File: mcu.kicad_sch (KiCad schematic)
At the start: 36 parts, among them Q1 BC817, Q2 BC817, SW1 SW_Push, SW2 SW_Push, SW3 SW_Push, U4 ESP32-S3-WROOM-1, U5 CP2102N-A02-GQFN28R

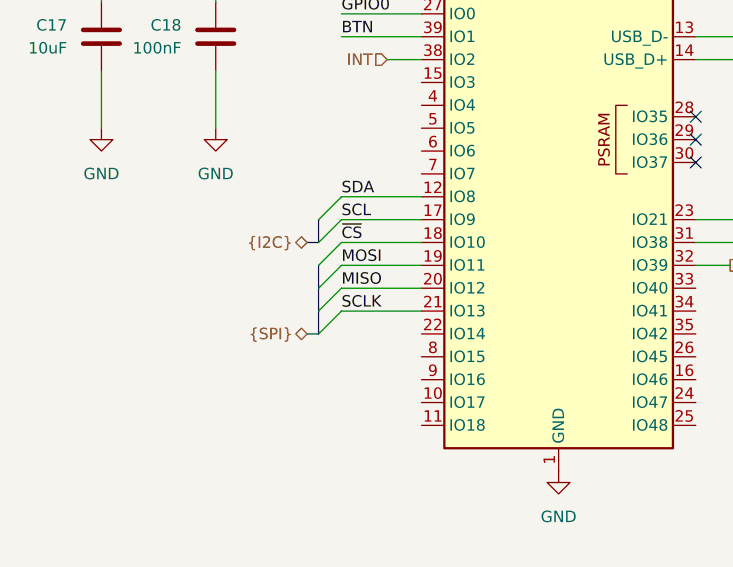
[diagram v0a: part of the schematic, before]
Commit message: Undo component replacement
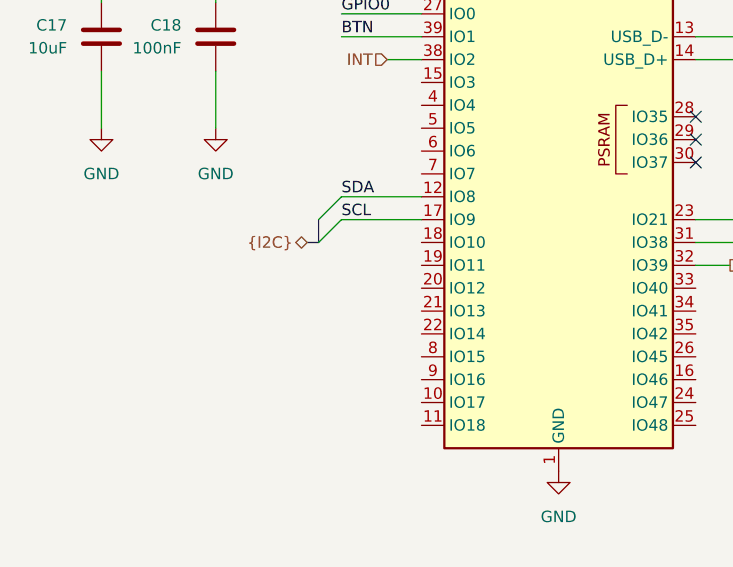
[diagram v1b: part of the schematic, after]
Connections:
- net MISO: no longer names the net of U4.20 (IO12)
- net MOSI: no longer names the net of U4.19 (IO11)
- net SCLK: no longer names the net of U4.21 (IO13)
- net ~{CS}: no longer names the net of U4.18 (IO10)

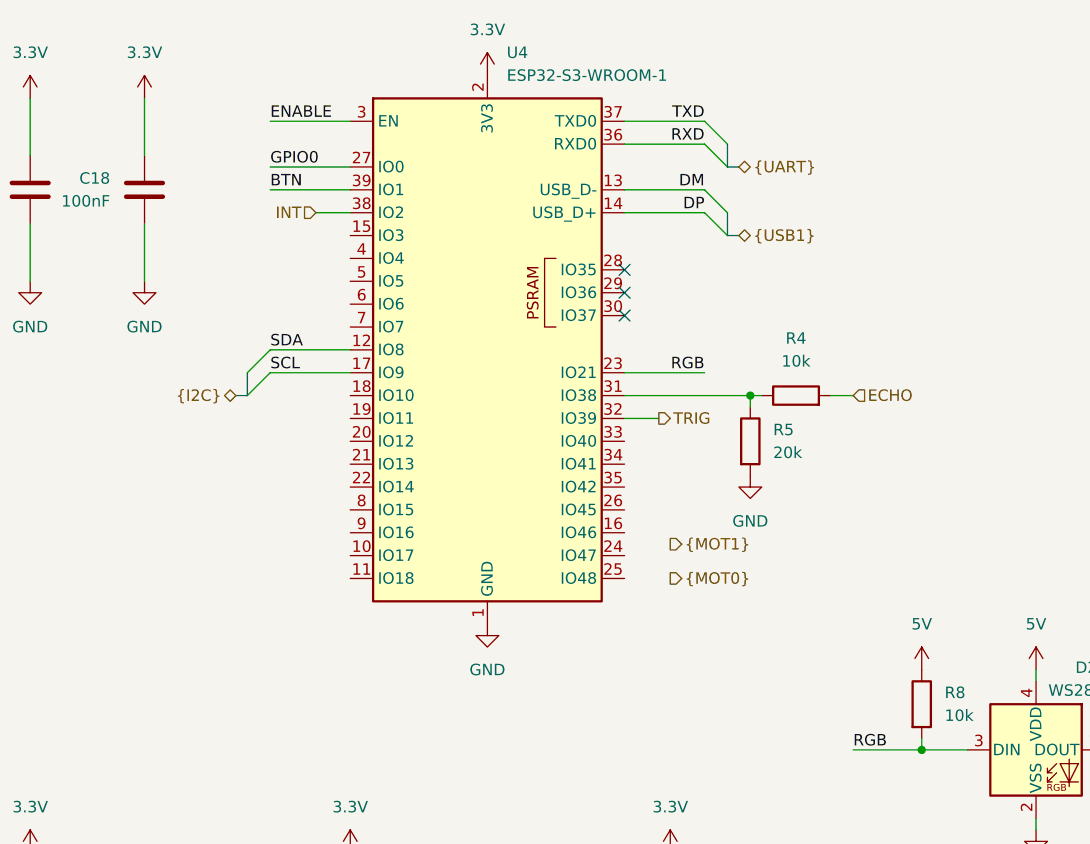
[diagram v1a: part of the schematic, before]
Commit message: Connect motor driver lines
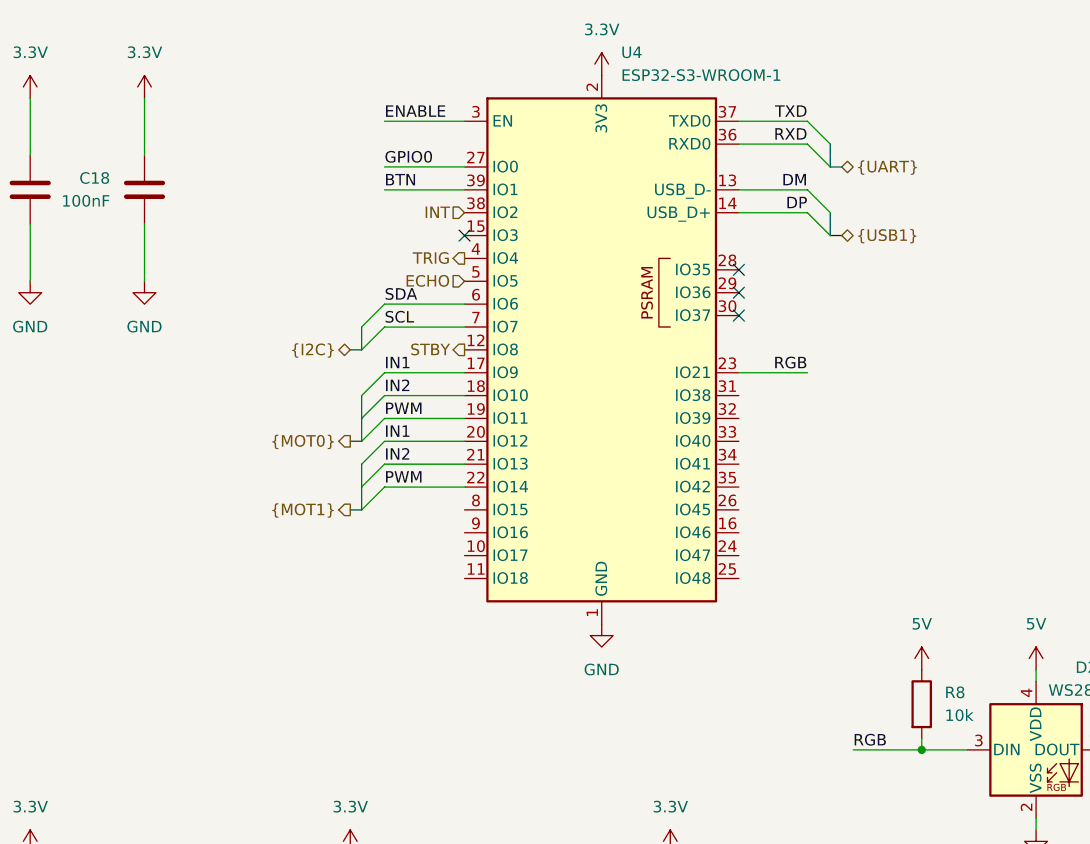
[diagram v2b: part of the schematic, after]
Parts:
- removed R4: 10k, symbol Device:R
- removed R5: 20k, symbol Device:R
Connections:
- net ECHO: now also U4.5 (IO5)
- net SCL: now also U4.7 (IO7); no longer U4.17 (IO9)
- net SDA: now also U4.6 (IO6); no longer U4.12 (IO8)
- net TRIG: now also U4.4 (IO4); no longer U4.32 (IO39)
- net IN2: now reaches U4.18 (IO10)
- net IN2: now also U4.21 (IO13)
- net PWM: now reaches U4.19 (IO11)
- net PWM: now also U4.22 (IO14)
- net IN1: now reaches U4.20 (IO12)
- net IN1: now also U4.17 (IO9)
- new net STBY: U4.12 (IO8)
- no-connect marks 13 -> 14
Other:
- moved on the sheet: U4

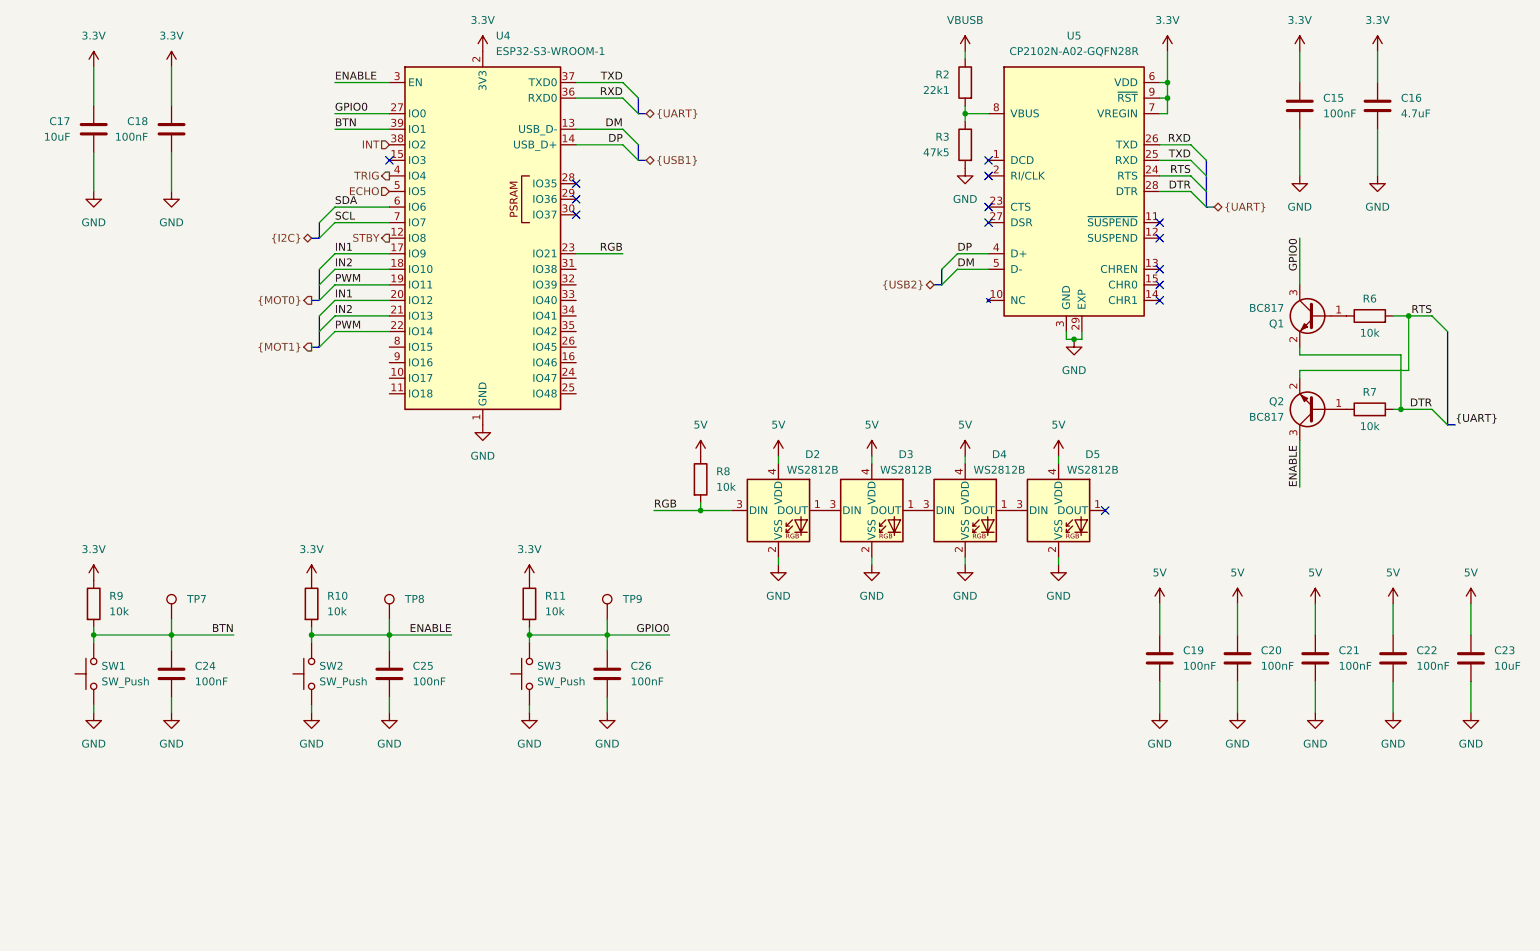
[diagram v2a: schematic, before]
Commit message: Add missing pull-up for CP2102
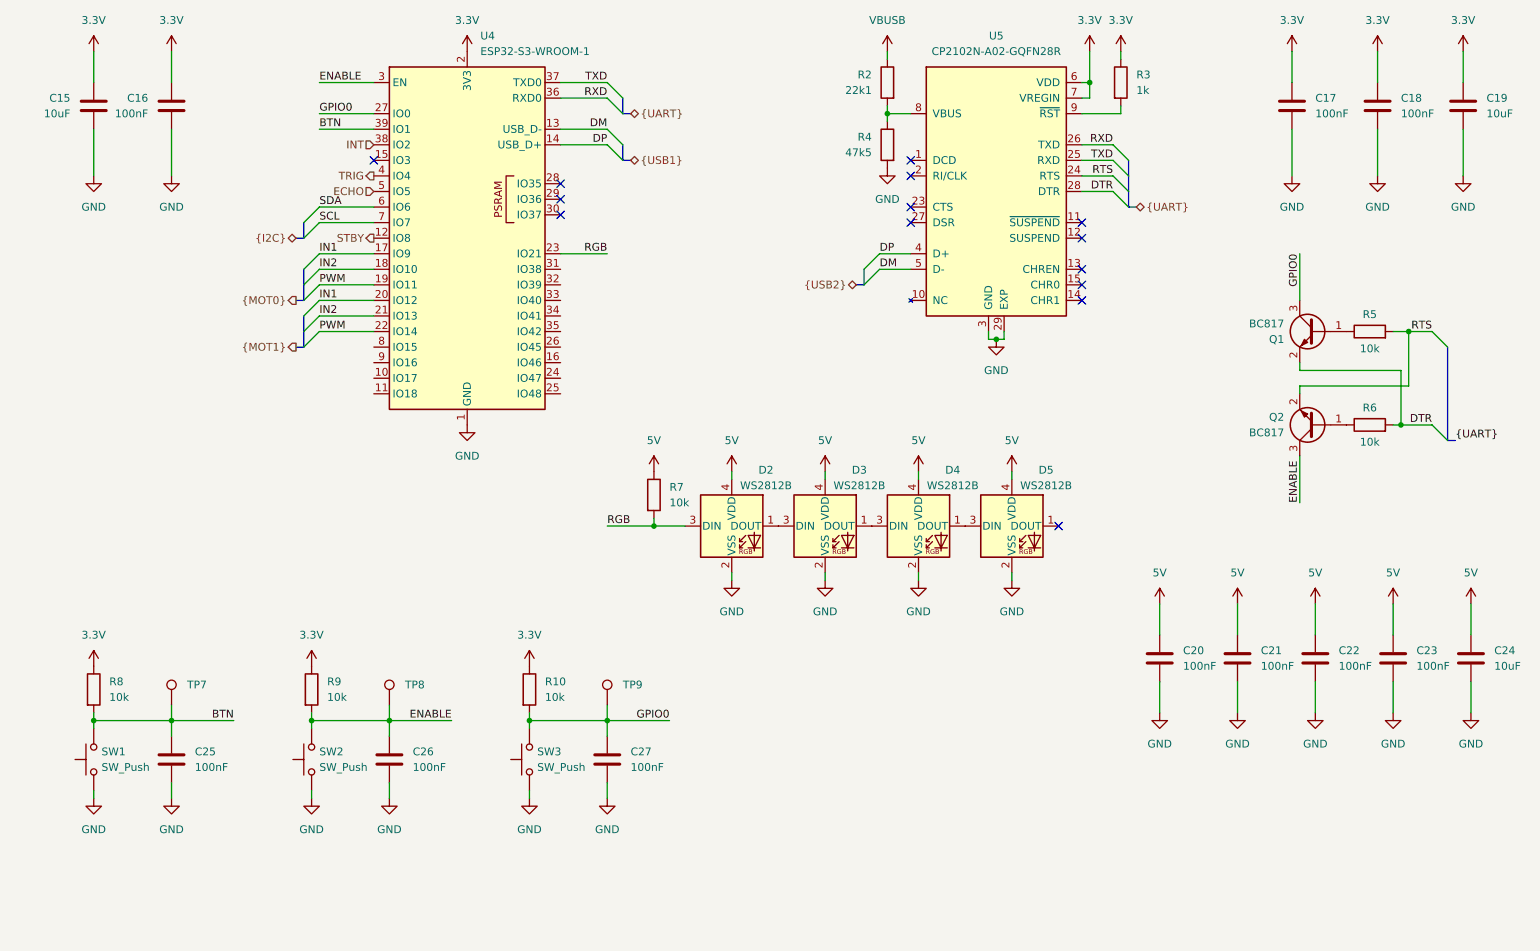
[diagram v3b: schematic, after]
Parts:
- added C18: 100nF, Capacitor_SMD:C_0402_1005Metric_Pad0.74x0.62mm_HandSolder, symbol Device:C
- added R3: 1k, symbol Device:R
- C19: renamed from C16; value 4.7uF -> 10uF
- renumbered C17 to C15, C18 to C16, C15 to C17, C19 to C20, C20 to C21, C21 to C22, C22 to C23, C23 to C24, C24 to C25, C25 to C26, C26 to C27, R11 to R10, R3 to R4, R6 to R5, R7 to R6, R8 to R7, R9 to R8, R10 to R9
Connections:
- net 3.3V: now also C18.1, R3.1; no longer U5.9 (~{RST})
- net GND: now also C18.2
- new net: R3.2, U5.9 (~{RST})
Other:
- moved on the sheet: C15, C16, C17, C19, C25, C26, C27, D2, D3, D4, D5, Q1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

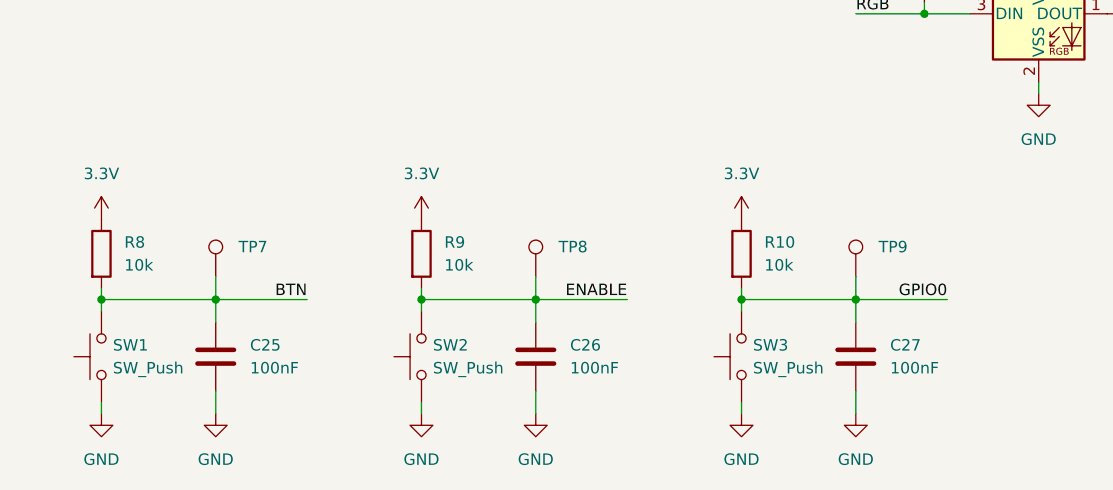
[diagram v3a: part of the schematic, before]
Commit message: Remove caps for BTN and GPIO0
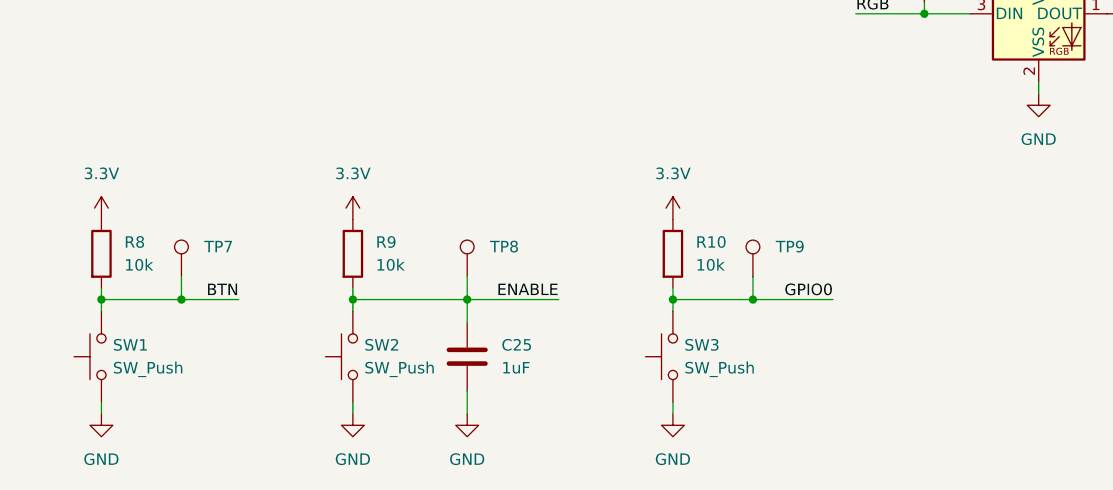
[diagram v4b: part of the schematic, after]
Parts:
- removed C25, C27: 100nF, Capacitor_SMD:C_0402_1005Metric_Pad0.74x0.62mm_HandSolder, symbol Device:C
- C25: renamed from C26; value 100nF -> 1uF
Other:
- moved on the sheet: C25, R10, R9, SW2, SW3, TP7, TP8, TP9

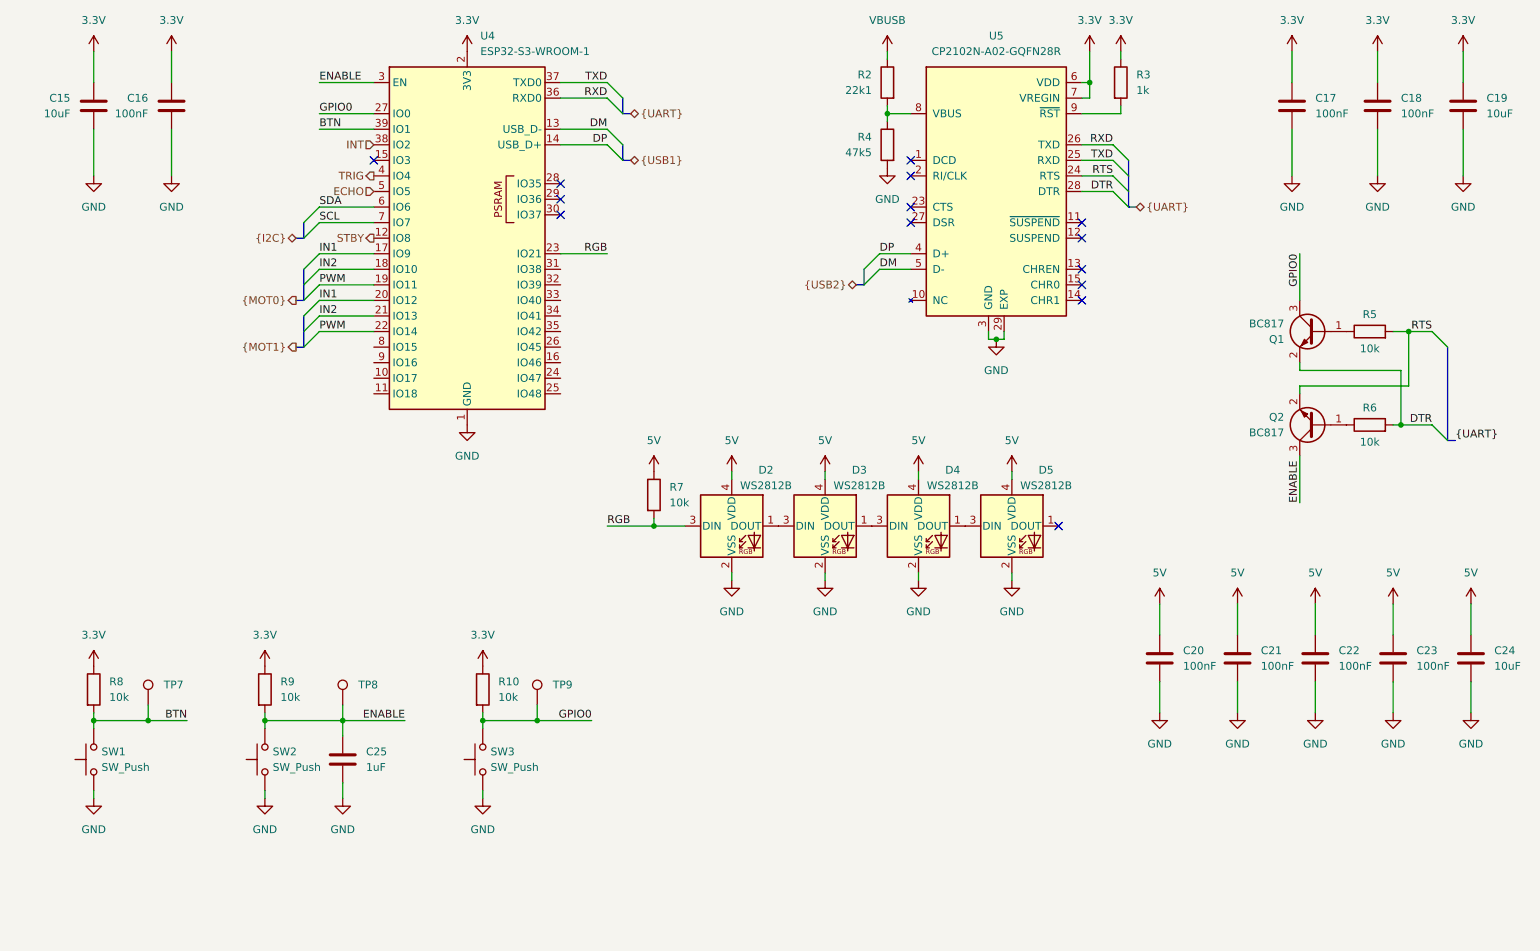
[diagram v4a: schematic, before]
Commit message: Add missing bus pull-ups
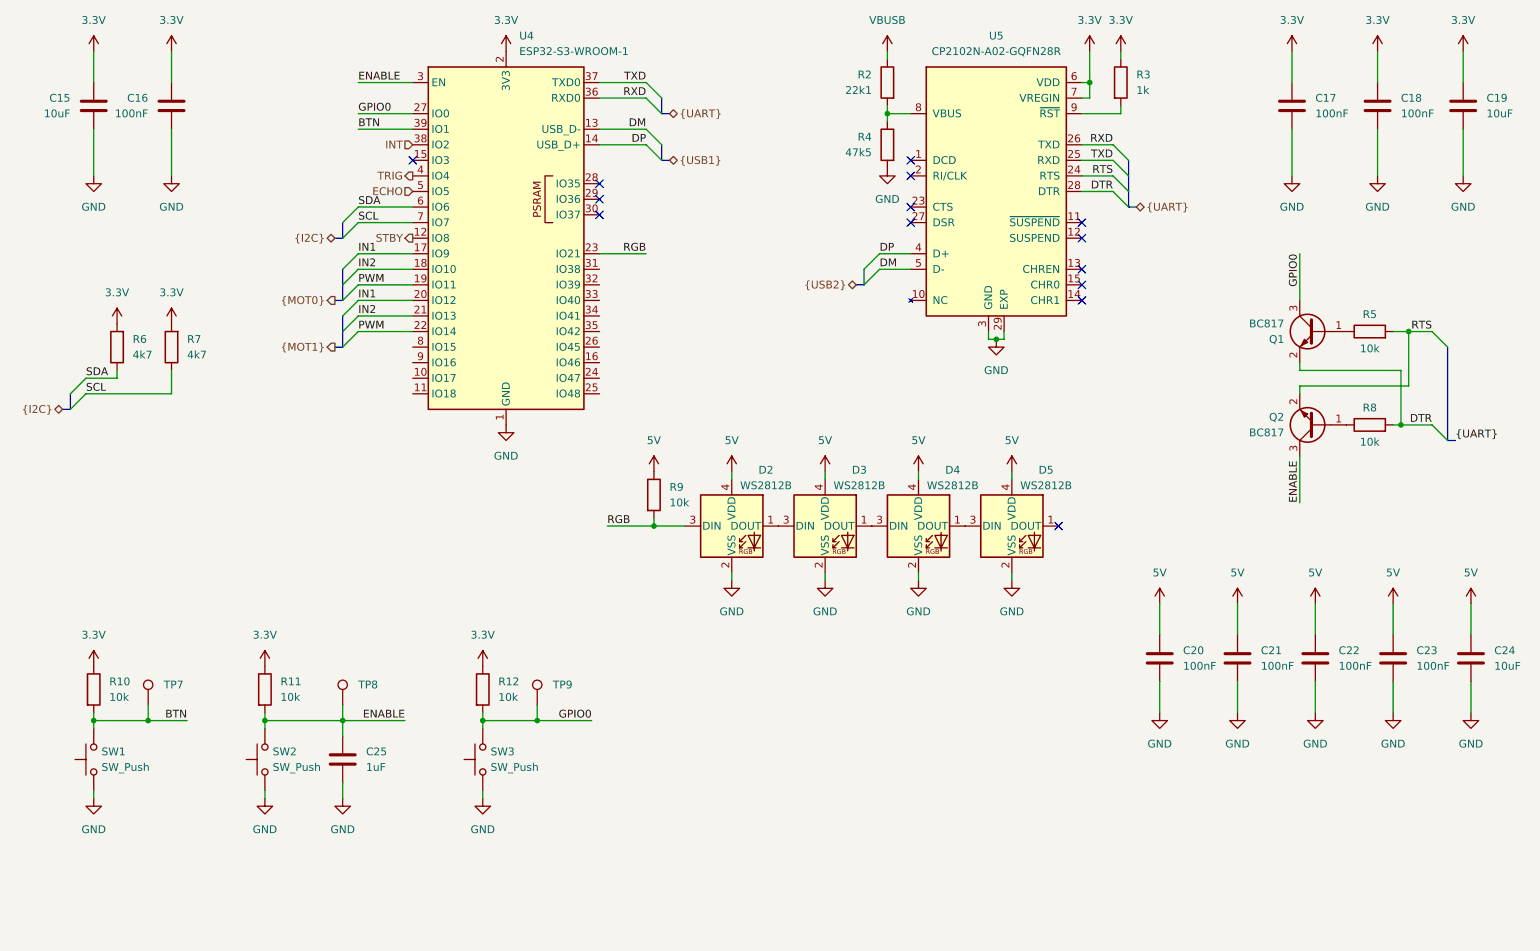
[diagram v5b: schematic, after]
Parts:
- added R6, R7: 4k7, symbol Device:R
- renumbered R8 to R10, R9 to R11, R10 to R12, R6 to R8, R7 to R9
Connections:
- net 3.3V: now also R6.2, R7.2
- net SCL: now also R7.1
- net SDA: now also R6.1
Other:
- moved on the sheet: U4
